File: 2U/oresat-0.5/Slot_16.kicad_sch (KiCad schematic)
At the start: 2 parts

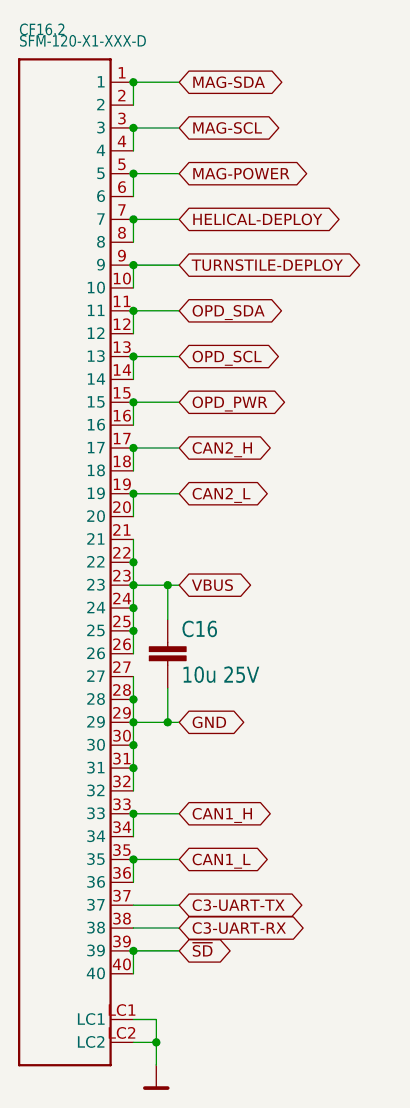
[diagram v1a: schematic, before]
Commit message: Fixed all (most) of the issues from Eagle imports
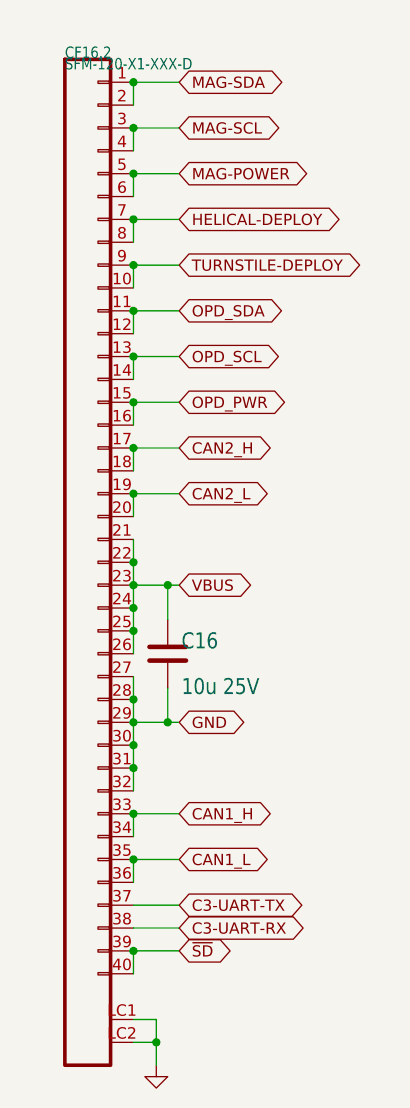
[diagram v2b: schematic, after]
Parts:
- C16: symbol oresat0-1u-backplane-eagle-import:C-EU1206-B -> Device:C
- CF16.2: symbol oresat-backplane-2u-eagle-import:SFM-120-X1-XXX-D -> oresat-connectors:J-SAMTEC-TFM-120-01-L-D-RA
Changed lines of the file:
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@@
 (kicad_sch (version 20211123) (generator eeschema)
   (paper "User" 490.22 254.406)
+  (junction (at 43.18 132.08) (diameter 0) (color 0 0 0 0)
+  )
+  (junction (at 43.18 157.48) (diameter 0) (color 0 0 0 0)
+  )
+  (junction (at 43.18 116.84) (diameter 0) (color 0 0 0 0)
+  )
   (junction (at 43.18 167.64) (diameter 0) (color 0 0 0 0)
   )
+  (junction (at 43.18 165.1) (diameter 0) (color 0 0 0 0)
+  )
+  (junction (at 43.18 193.04) (diameter 0) (color 0 0 0 0)
+  )
+  (junction (at 43.18 127) (diameter 0) (color 0 0 0 0)
+  )
+  (junction (at 43.18 187.96) (diameter 0) (color 0 0 0 0)
+  )
+  (junction (at 43.18 142.24) (diameter 0) (color 0 0 0 0)
+  )
+  (junction (at 43.18 185.42) (diameter 0) (color 0 0 0 0)
+  )
   (junction (at 43.18 111.76) (diameter 0) (color 0 0 0 0)
   )
+  (junction (at 43.18 137.16) (diameter 0) (color 0 0 0 0)
+  )
+  (junction (at 43.18 180.34) (diameter 0) (color 0 0 0 0)
+  )
   (junction (at 43.18 198.12) (diameter 0) (color 0 0 0 0)
   )
+  (junction (at 43.18 152.4) (diameter 0) (color 0 0 0 0)
+  )
+  (junction (at 43.18 170.18) (diameter 0) (color 0 0 0 0)
+  )
+  (junction (at 45.72 218.44) (diameter 0) (color 0 0 0 0)
+  )
+  (junction (at 46.99 167.64) (diameter 0) (color 0 0 0 0)
+  )
+  (junction (at 43.18 147.32) (diameter 0) (color 0 0 0 0)
+  )
+  (junction (at 46.99 182.88) (diameter 0) (color 0 0 0 0)
+  )
+  (junction (at 43.18 182.88) (diameter 0) (color 0 0 0 0)
+  )
+  (junction (at 43.18 208.28) (diameter 0) (color 0 0 0 0)
+  )
   (junction (at 43.18 121.92) (diameter 0) (color 0 0 0 0)
   )
-  (junction (at 43.18 165.1) (diameter 0) (color 0 0 0 0)
-  )
-  (junction (at 43.18 180.34) (diameter 0) (color 0 0 0 0)
-  )
-  (junction (at 43.18 187.96) (diameter 0) (color 0 0 0 0)
-  )
-  (junction (at 43.18 132.08) (diameter 0) (color 0 0 0 0)
-  )
   (junction (at 43.18 172.72) (diameter 0) (color 0 0 0 0)
   )
-  (junction (at 43.18 157.48) (diameter 0) (color 0 0 0 0)
-  )
-  (junction (at 43.18 127) (diameter 0) (color 0 0 0 0)
-  )
-  (junction (at 43.18 137.16) (diameter 0) (color 0 0 0 0)
-  )
-  (junction (at 45.72 218.44) (diameter 0) (color 0 0 0 0)
-  )
-  (junction (at 46.99 167.64) (diameter 0) (color 0 0 0 0)
-  )
-  (junction (at 43.18 142.24) (diameter 0) (color 0 0 0 0)
-  )
-  (junction (at 46.99 182.88) (diameter 0) (color 0 0 0 0)
-  )
-  (junction (at 43.18 185.42) (diameter 0) (color 0 0 0 0)
-  )
-  (junction (at 43.18 182.88) (diameter 0) (color 0 0 0 0)
-  )
-  (junction (at 43.18 152.4) (diameter 0) (color 0 0 0 0)
-  )
-  (junction (at 43.18 193.04) (diameter 0) (color 0 0 0 0)
-  )
-  (junction (at 43.18 170.18) (diameter 0) (color 0 0 0 0)
-  )
-  (junction (at 43.18 208.28) (diameter 0) (color 0 0 0 0)
-  )
-  (junction (at 43.18 116.84) (diameter 0) (color 0 0 0 0)
-  )
-  (junction (at 43.18 147.32) (diameter 0) (color 0 0 0 0)
-  )
   (wire (pts (xy 48.26 147.32) (xy 43.18 147.32))
     (stroke (width 0) (type default) (color 0 0 0 0))
@@
     (stroke (width 0) (type default) (color 0 0 0 0))
   )
+  (wire (pts (xy 43.18 185.42) (xy 43.18 187.96))
+    (stroke (width 0) (type default) (color 0 0 0 0))
+  )
   (wire (pts (xy 46.99 167.64) (xy 46.99 171.45))
     (stroke (width 0) (type default) (color 0 0 0 0))
@@
     (stroke (width 0) (type default) (color 0 0 0 0))
   )
-  (wire (pts (xy 43.18 185.42) (xy 43.18 187.96))
+  (wire (pts (xy 43.18 167.64) (xy 43.18 170.18))
+    (stroke (width 0) (type default) (color 0 0 0 0))
+  )
+  (wire (pts (xy 43.18 162.56) (xy 43.18 165.1))
     (stroke (width 0) (type default) (color 0 0 0 0))
   )
@@
     (stroke (width 0) (type default) (color 0 0 0 0))
   )
+  (wire (pts (xy 43.18 172.72) (xy 43.18 175.26))
+    (stroke (width 0) (type default) (color 0 0 0 0))
+  )
   (wire (pts (xy 48.26 208.28) (xy 43.18 208.28))
     (stroke (width 0) (type default) (color 0 0 0 0))
   )
+  (wire (pts (xy 43.18 180.34) (xy 43.18 182.88))
+    (stroke (width 0) (type default) (color 0 0 0 0))
+  )
   (wire (pts (xy 46.99 182.88) (xy 43.18 182.88))
     (stroke (width 0) (type default) (color 0 0 0 0))
   )
+  (wire (pts (xy 43.18 182.88) (xy 43.18 185.42))
+    (stroke (width 0) (type default) (color 0 0 0 0))
+  )
   (wire (pts (xy 43.18 127) (xy 43.18 129.54))
     (stroke (width 0) (type default) (color 0 0 0 0))
@@
     (stroke (width 0) (type default) (color 0 0 0 0))
   )
+  (wire (pts (xy 43.18 177.8) (xy 43.18 180.34))
+    (stroke (width 0) (type default) (color 0 0 0 0))
+  )
   (wire (pts (xy 48.26 142.24) (xy 43.18 142.24))
     (stroke (width 0) (type default) (color 0 0 0 0))
@@
     (stroke (width 0) (type default) (color 0 0 0 0))
   )
+  (wire (pts (xy 43.18 170.18) (xy 43.18 172.72))
+    (stroke (width 0) (type default) (color 0 0 0 0))
+  )
   (wire (pts (xy 48.26 182.88) (xy 46.99 182.88))
     (stroke (width 0) (type default) (color 0 0 0 0))
@@
     (stroke (width 0) (type default) (color 0 0 0 0))
   )
-  (wire (pts (xy 43.18 172.72) (xy 43.18 175.26))
+  (wire (pts (xy 43.18 187.96) (xy 43.18 190.5))
     (stroke (width 0) (type default) (color 0 0 0 0))
   )
@@
     (stroke (width 0) (type default) (color 0 0 0 0))
   )
+  (wire (pts (xy 48.26 203.2) (xy 43.18 203.2))
+    (stroke (width 0) (type default) (color 0 0 0 0))
+  )
   (wire (pts (xy 43.18 165.1) (xy 43.18 167.64))
     (stroke (width 0) (type default) (color 0 0 0 0))
   )
-  (wire (pts (xy 48.26 203.2) (xy 43.18 203.2))
-    (stroke (width 0) (type default) (color 0 0 0 0))
-  )
   (wire (pts (xy 43.18 198.12) (xy 43.18 200.66))
     (stroke (width 0) (type default) (color 0 0 0 0))
@@
     (stroke (width 0) (type default) (color 0 0 0 0))
   )
-  (wire (pts (xy 43.18 162.56) (xy 43.18 165.1))
-    (stroke (width 0) (type default) (color 0 0 0 0))
-  )
-  (wire (pts (xy 43.18 170.18) (xy 43.18 172.72))
-    (stroke (width 0) (type default) (color 0 0 0 0))
-  )
-  (wire (pts (xy 43.18 167.64) (xy 43.18 170.18))
-    (stroke (width 0) (type default) (color 0 0 0 0))
-  )
   (wire (pts (xy 45.72 218.44) (xy 45.72 220.98))
     (stroke (width 0) (type default) (color 0 0 0 0))
   )
-  (wire (pts (xy 43.18 182.88) (xy 43.18 185.42))
-    (stroke (width 0) (type default) (color 0 0 0 0))
-  )
-  (wire (pts (xy 43.18 187.96) (xy 43.18 190.5))
-    (stroke (width 0) (type default) (color 0 0 0 0))
-  )
   (wire (pts (xy 48.26 132.08) (xy 43.18 132.08))
     (stroke (width 0) (type default) (color 0 0 0 0))
   )
-  (wire (pts (xy 43.18 177.8) (xy 43.18 180.34))
-    (stroke (width 0) (type default) (color 0 0 0 0))
-  )
   (wire (pts (xy 48.26 137.16) (xy 43.18 137.16))
     (stroke (width 0) (type default) (color 0 0 0 0))
@@
     (stroke (width 0) (type default) (color 0 0 0 0))
   )
-  (wire (pts (xy 43.18 180.34) (xy 43.18 182.88))
-    (stroke (width 0) (type default) (color 0 0 0 0))
-  )
   (wire (pts (xy 43.18 147.32) (xy 43.18 149.86))
     (stroke (width 0) (type default) (color 0 0 0 0))
@@
     )
   )
-  (symbol (lib_id "oresat-backplane-2u-eagle-import:GND") (at 45.72 220.98 0) (unit 1)
+  (symbol (lib_id "power:GND") (at 45.72 220.98 0) (unit 1)
     (in_bom yes) (on_board yes)
     (property "Reference" "#GND0115" (id 0) (at 45.72 220.98 0)
@@
     (pin "1")
   )
-  (symbol (lib_id "oresat-backplane-2u-eagle-import:SFM-120-X1-XXX-D") (at 33.02 157.48 0) (unit 1)
+  (symbol (lib_id "oresat-connectors:J-SAMTEC-TFM-120-01-L-D-RA") (at 38.1 160.02 0) (unit 1)
     (in_bom yes) (on_board yes)
-    (property "Reference" "CF16.2" (id 0) (at 30.48 106.68 0)
+    (property "Reference" "CF16.2" (id 0) (at 35.56 109.22 0)
       (effects (font (size 1.27 1.0795)) (justify left bottom))
     )
-    (property "Value" "SFM-120-X1-XXX-D" (id 1) (at 30.48 107.95 0)
+    (property "Value" "SFM-120-X1-XXX-D" (id 1) (at 35.56 110.49 0)
       (effects (font (size 1.27 1.0795)) (justify left bottom))
     )
-    (property "Footprint" "oresat-connectors:J-SAMTEC-SFM-120-X1-XXX-D" (id 2) (at 33.02 157.48 0)
-      (effects (font (size 1.27 1.27)) hide)
-    )
-    (property "Datasheet" "" (id 3) (at 33.02 157.48 0)
+    (property "Footprint" "oresat-connectors:J-SAMTEC-SFM-120-X1-XXX-D" (id 2) (at 38.1 160.02 0)
+      (effects (font (size 1.27 1.27)) hide)
+    )
+    (property "Datasheet" "" (id 3) (at 38.1 160.02 0)
       (effects (font (size 1.27 1.27)) hide)
     )
@@
     (pin "LC2")
   )
-  (symbol (lib_id "oresat0-1u-backplane-eagle-import:C-EU1206-B") (at 46.99 173.99 0) (unit 1)
+  (symbol (lib_id "Device:C") (at 46.99 175.26 0) (unit 1)
     (in_bom yes) (on_board yes)
-    (property "Reference" "C16" (id 0) (at 48.514 173.609 0)
+    (property "Reference" "C16" (id 0) (at 48.514 174.879 0)
       (effects (font (size 1.778 1.5113)) (justify left bottom))
     )
-    (property "Value" "10u 25V" (id 1) (at 48.514 178.689 0)
+    (property "Value" "10u 25V" (id 1) (at 48.514 179.959 0)
       (effects (font (size 1.778 1.5113)) (justify left bottom))
     )
-    (property "Footprint" "Capacitor_SMD:C_1206_3216Metric" (id 2) (at 46.99 173.99 0)
-      (effects (font (size 1.27 1.27)) hide)
-    )
-    (property "Datasheet" "" (id 3) (at 46.99 173.99 0)
-      (effects (font (size 1.27 1.27)) hide)
-    )
+    (property "Footprint" "Capacitor_SMD:C_1206_3216Metric" (id 2) (at 46.99 175.26 0)
+      (effects (font (size 1.27 1.27)) hide)
+    )
+    (property "Datasheet" "" (id 3) (at 46.99 175.26 0)
+      (effects (font (size 1.27 1.27)) hide)
+    )

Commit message: Moved entire schematic to single page
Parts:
- removed C16: 10u 25V, Capacitor_SMD:C_1206_3216Metric, symbol Device:C
- removed CF16.2: SFM-120-X1-XXX-D, oresat-connectors:J-SAMTEC-SFM-120-X1-XXX-D, symbol oresat-connectors:J-SAMTEC-TFM-120-01-L-D-RA
